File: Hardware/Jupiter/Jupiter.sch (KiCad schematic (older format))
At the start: 65 parts

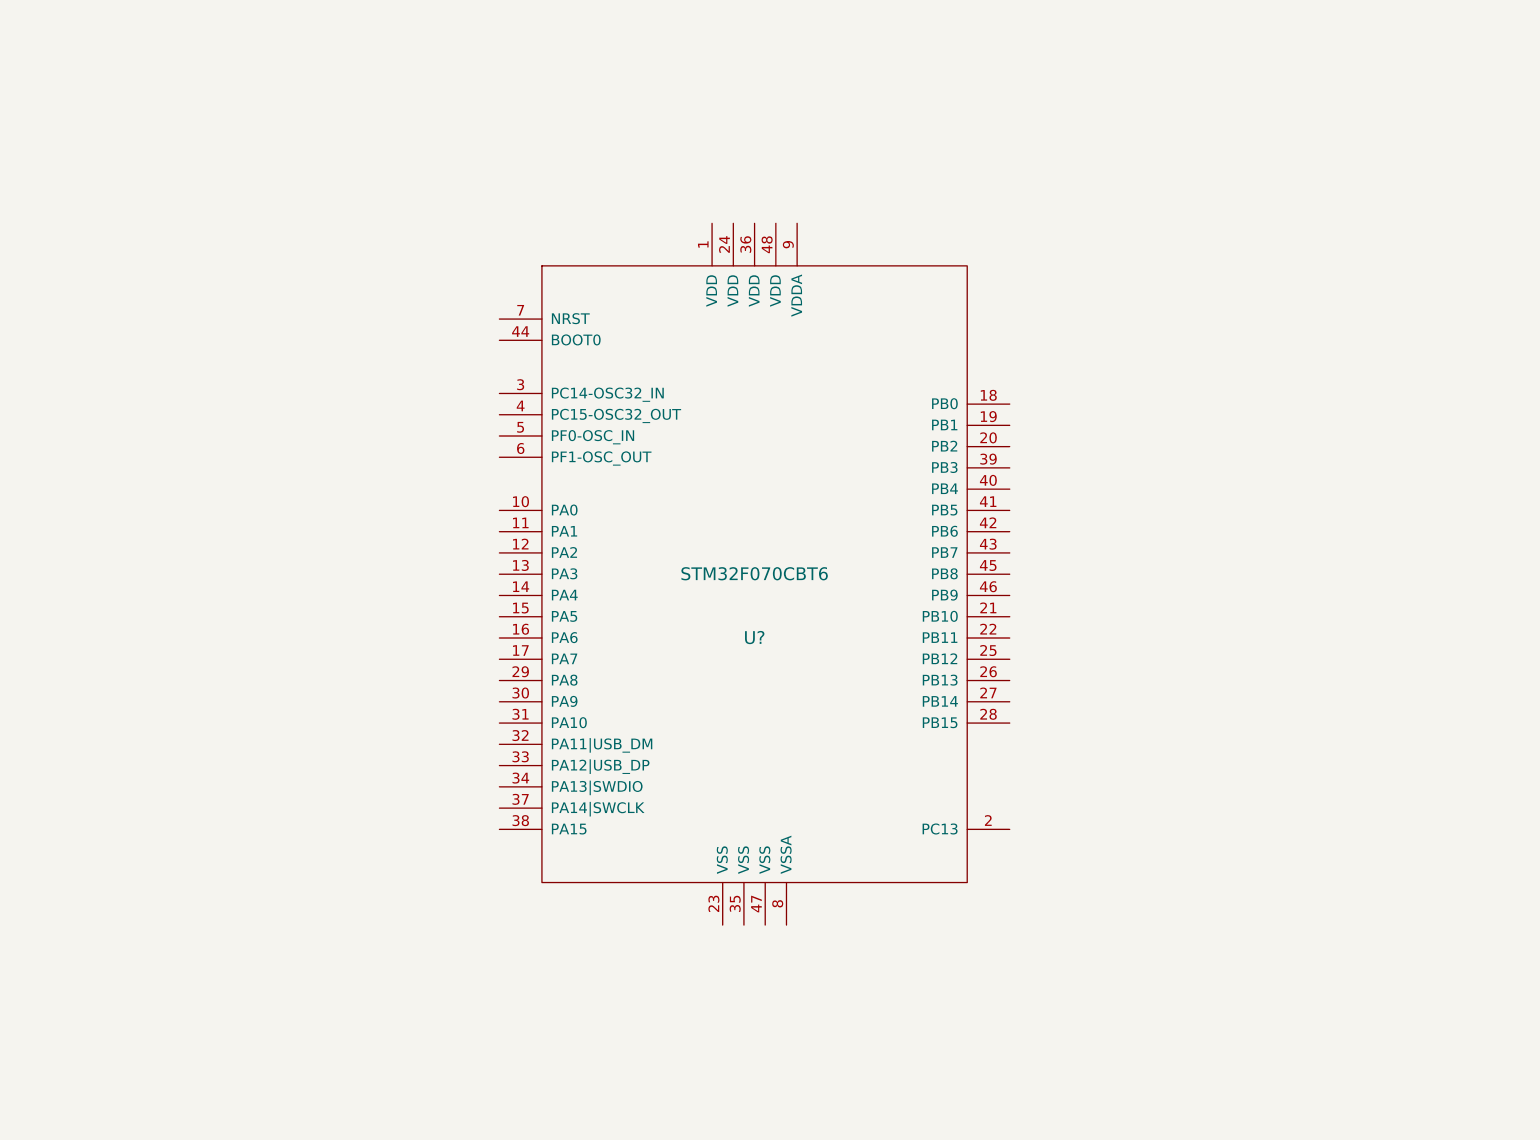
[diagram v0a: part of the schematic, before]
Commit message: Add a uC for interfacing with an Atari Jaguar controller.
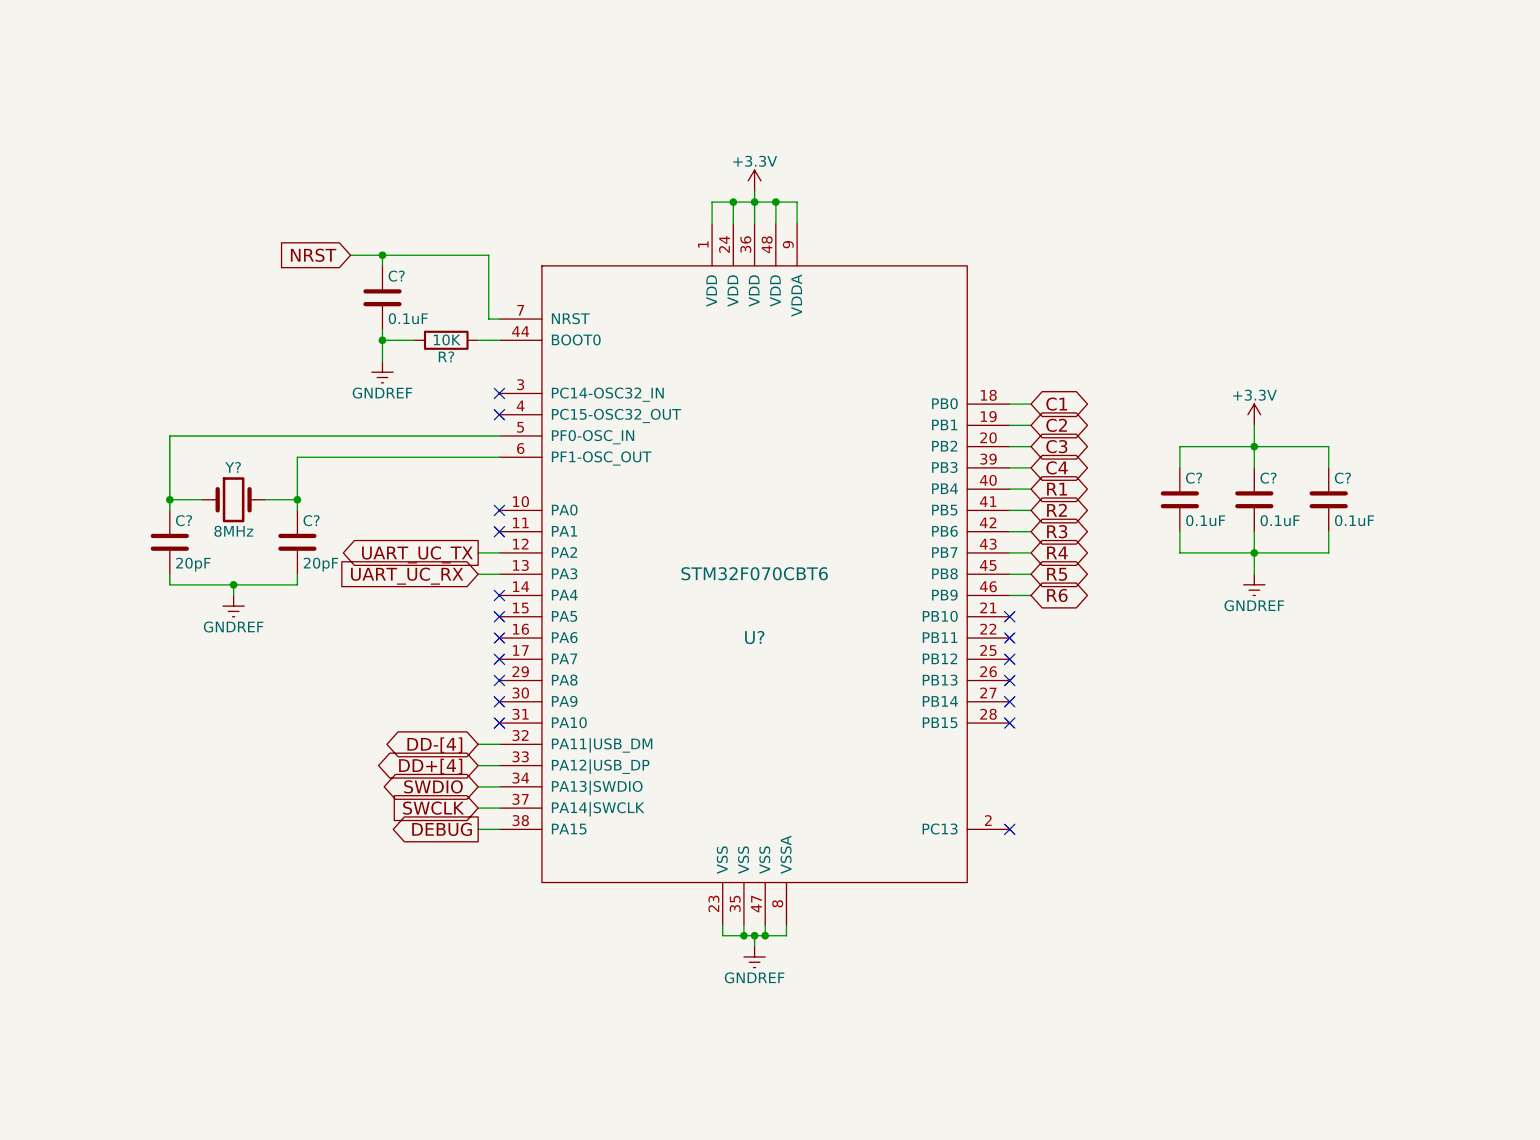
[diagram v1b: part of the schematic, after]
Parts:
- added C? (x4): 0.1uF, symbol C
- added C? (x2): 20pF, symbol C
- added R?: 10K, symbol R
- added Y?: 8MHz, symbol Crystal
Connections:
- net +3V3: now also U?.1 (VDD), U?.24 (VDD), U?.36 (VDD), U?.48 (VDD), U?.9 (VDDA), C?.1, C?.1, C?.1
- net DD+[4]: now also U?.33 (PA12|USB_DP)
- net DD-[4]: now also U?.32 (PA11|USB_DM)
- net GNDREF: now also U?.23 (VSS), U?.35 (VSS), U?.47 (VSS), U?.8 (VSSA), C?.2, C?.2, C?.2, C?.2, C?.2, C?.2, R?.2
- net UART_UC_TX: now reaches U?.12 (PA2)
- net UART_UC_RX: now reaches U?.13 (PA3)
- net C1: now reaches U?.18 (PB0)
- net C2: now reaches U?.19 (PB1)
- net C3: now reaches U?.20 (PB2)
- net SWDIO: now reaches U?.34 (PA13|SWDIO)
- net SWCLK: now reaches U?.37 (PA14|SWCLK)
- net DEBUG: now reaches U?.38 (PA15)
- net C4: now reaches U?.39 (PB3)
- net R1: now reaches U?.40 (PB4)
- net R2: now reaches U?.41 (PB5)
- net R3: now reaches U?.42 (PB6)
- net R4: now reaches U?.43 (PB7)
- net at U?.44 (BOOT0): now also R?.1
- net R5: now reaches U?.45 (PB8)
- net R6: now reaches U?.46 (PB9)
- net at U?.5 (PF0-OSC_IN): now also C?.1, Y?.1
- net at U?.6 (PF1-OSC_OUT): now also C?.1, Y?.2
- net NRST: now reaches U?.7 (NRST)
- net NRST: now also C?.1
- no-connect marks 5 -> 23

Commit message: Add labels to uC for Jaguar controller interface.
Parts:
- added D?: LED, symbol LED
- added R?: 649, symbol R
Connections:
- net GNDREF: now also D?.1 (K)
- net DEBUG: no longer names the net of U?.38 (PA15)
- net DEBUG: now also R?.1
- new net: D?.2 (A), R?.2
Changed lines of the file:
@@
 Text GLabel 7450 7550 0    60   Input ~ 0
 SWCLK
-Text GLabel 7450 7650 0    60   Output ~ 0
-DEBUG
 Wire Wire Line
 	7450 7650 7550 7650
@@
 	1    0    0    -1
 $EndComp
+$Comp
+L R R?
+U 1 1 5B6D12A7
+P 7300 7650
+F 0 "R?" V 7380 7650 50  0000 C CNN
+F 1 "649" V 7300 7650 50  0000 C CNN
+F 2 "" V 7230 7650 50  0001 C CNN
+F 3 "" H 7300 7650 50  0001 C CNN
+	1    7300 7650
+	0    1    1    0
+$EndComp
+$Comp
+L LED D?
+U 1 1 5B6D1BF2
+P 7050 7900
+F 0 "D?" H 7050 8000 50  0000 C CNN
+F 1 "LED" H 7050 7800 50  0000 C CNN
+F 2 "" H 7050 7900 50  0001 C CNN
+F 3 "" H 7050 7900 50  0001 C CNN
+	1    7050 7900
+	0    -1   -1   0
+$EndComp
+Wire Wire Line
+	7150 7650 7050 7650
+Wire Wire Line
+	7050 7650 7050 7750
+$Comp
+L GNDREF #PWR?
+U 1 1 5B6D1EA0
+P 7050 8200
+F 0 "#PWR?" H 7050 7950 50  0001 C CNN
+F 1 "GNDREF" H 7050 8050 50  0000 C CNN
+F 2 "" H 7050 8200 50  0001 C CNN
+F 3 "" H 7050 8200 50  0001 C CNN
+	1    7050 8200
+	1    0    0    -1
+$EndComp
+Wire Wire Line
+	7050 8200 7050 8050
 $EndSCHEMATC

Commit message: Connect up external facing ports such as debug/programming headers and Ethernet.
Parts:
- added C? (x6): 0.1uF, symbol C
- added J?: DB15_FEMALE_HighDensity, symbol DB15_FEMALE_HighDensity
- added J?: CONN_01X05, symbol CONN_01X05
- added J?: CONN_01X02, symbol CONN_01X02
- added L?: Ferrite_Bead, symbol Ferrite_Bead
- added R? (x2): 649, symbol R
- added R? (x4): 50, symbol R
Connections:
- net +3V3: now also C?.1, C?.1, C?.1, C?.1, J?.1 (P1), J?.7, L?.1
- net C1: now also J?.1
- net C2: now also J?.2
- net C3: now also J?.3
- net C4: now also J?.4
- net GNDREF: now also J?.13 (SHIELD), J?.8, C?.2, C?.2, C?.2, C?.2, C?.2, C?.2, J?.3 (P3), J?.9, R?.2, R?.2
- net LEDA: now also J?.GA (LEDG_A)
- net LEDB: now also J?.YA (LEDY_A)
- net NRST: now also J?.5 (P5)
- net R1: now also J?.6
- net R2: now also J?.10
- net R3: now also J?.11
- net R4: now also J?.12
- net R5: now also J?.13
- net R6: now also J?.14
- net SWCLK: now also J?.2 (P2)
- net SWDIO: now also J?.4 (P4)
- net TPIN+: now also J?.6 (RD-), R?.2
- net TPIN-: now also J?.4 (RD+), R?.1
- net TPOUT+: now also J?.1 (TD+), R?.1
- net TPOUT-: now also J?.3 (TD-), R?.2
- net UART_UC_RX: now also J?.1 (P1)
- net UART_UC_TX: now also J?.2 (P2)
- net at J?.2 (TCT): now also C?.1, L?.2, R?.1, R?.2
- net at J?.5 (RCT): now also C?.1, R?.1, R?.2
- net at J?.GK (LEDG_K): now also R?.1
- net at J?.YK (LEDY_K): now also R?.1
- no-connect marks 23 -> 26
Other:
- moved on the sheet: C?, D?, J?, L?, R?, RN?, U?, Y?

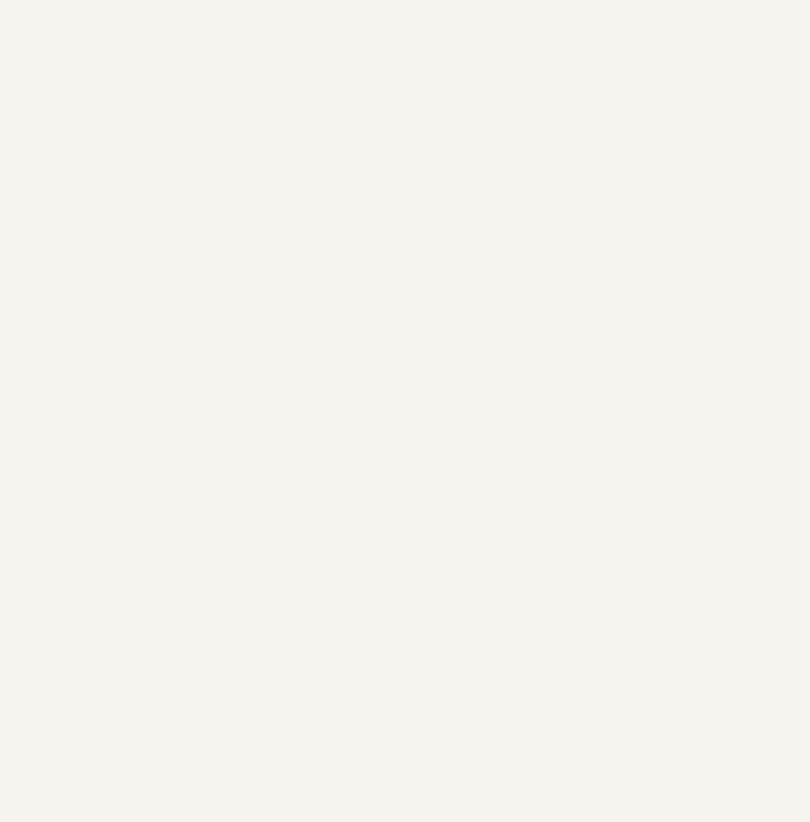
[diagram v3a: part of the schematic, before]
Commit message: Add HDMI port to the component and footprint libraries.
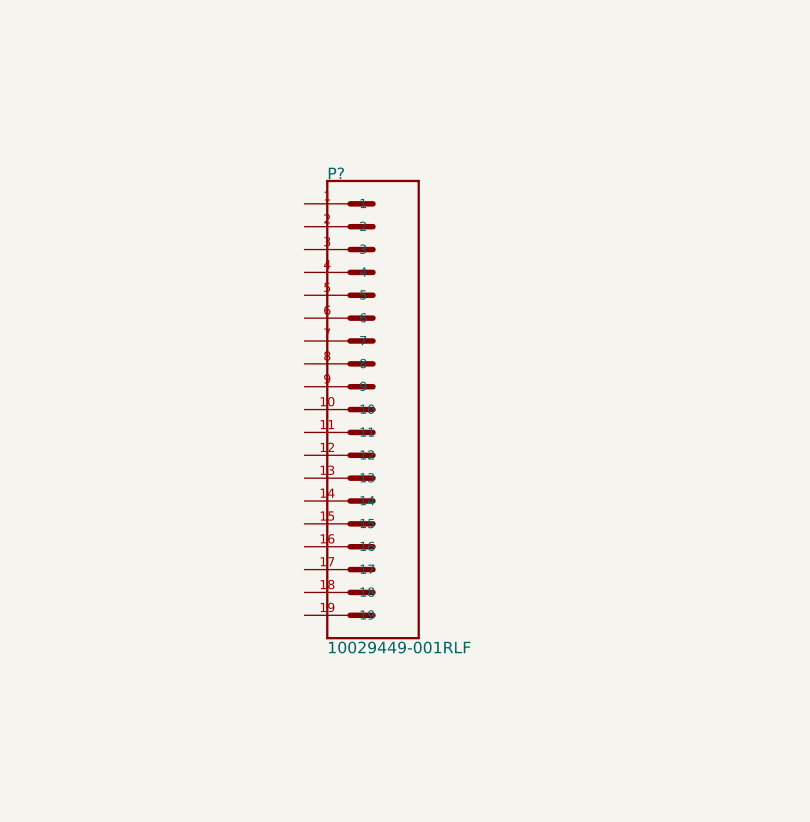
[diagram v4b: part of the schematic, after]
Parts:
- added P?: 10029449-001RLF, FCI_10029449-001RLF, symbol 10029449-001RLF
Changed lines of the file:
@@
 LIBS:503182-1852
 LIBS:MP2149
+LIBS:10029449-001RLF
 LIBS:Jupiter-cache
 EELAYER 25 0
@@
 	19300 2350 19300 3400
 Connection ~ 19650 3400
+$Comp
+L 10029449-001RLF P?
+U 1 1 5B6B6B8C
+P 8850 6750
+F 0 "P?" H 8650 7752 50  0000 L BNN
+F 1 "10029449-001RLF" H 8650 5678 50  0000 L BNN
+F 2 "FCI_10029449-001RLF" H 8850 6750 50  0001 L BNN
+F 3 "10029449-001RLF" H 8850 6750 50  0001 L BNN
+F 4 "None" H 8850 6750 50  0001 L BNN "Field4"
+F 5 "https://www.digikey.com/product-detail/en/amphenol-fci/10029449-001RLF/609-1010-1-ND/1002823?utm_source=snapeda&utm_medium=aggregator&utm_campaign=symbol" H 8850 6750 50  0001 L BNN "Field5"
+F 6 "609-1010-1-ND" H 8850 6750 50  0001 L BNN "Field6"
+F 7 "Amphenol" H 8850 6750 50  0001 L BNN "Field7"
+F 8 "Conn HDMI RCP 19 POS 0.5mm Solder RA SMD 19 Terminal 1 Port T/R" H 8850 6750 50  0001 L BNN "Field8"
+	1    8850 6750
+	1    0    0    -1
+$EndComp
 $EndSCHEMATC
